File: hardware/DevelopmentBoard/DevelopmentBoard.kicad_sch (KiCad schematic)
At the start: 0 parts

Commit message: Update development board hardware schematic
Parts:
- added A1: ~, symbol ComponentLibrary:ESP32_Devkitc_V4
- added J1: 12V connector, symbol Connector:Barrel_Jack
- added J2: Servo 1, symbol Connector:Conn_01x03_Pin
- added J3: Servo 2, symbol Connector:Conn_01x03_Pin
- added J4: JTAG, symbol Connector_Generic:Conn_02x10_Odd_Even
- added Pot1: 10k, symbol Device:R_Potentiometer
- added R1, R2, R3, R4: 10k, symbol Device:R
- added SW1, SW2, SW3, SW4: SW_Push, symbol Switch:SW_Push
- added TrimPot1, TrimPot2: 10k, symbol Device:R_Potentiometer_Trim
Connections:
- new net: J1.1, J2.2 (Pin_2), J3.2 (Pin_2)
- new net: A1.30 (18), J3.3 (Pin_3)
- new net: A1.10 (26), TrimPot1.2
- new net: A1.11 (27), TrimPot2.2
- new net: A1.12 (14), J4.7 (Pin_7)
- new net: A1.13 (12), J4.5 (Pin_5)
- new net: A1.15 (13), J4.9 (Pin_9)
- new net: A1.2 (EN), J4.3 (Pin_3)
- new net: A1.23 (15), J4.13 (Pin_13)
- new net: A1.3 (VP), R1.2, SW1.2
- new net: A1.31 (19), J2.3 (Pin_3)
- new net: A1.4 (VN), R2.2, SW2.2
- new net: A1.5 (34), R3.2, SW3.2
- new net: A1.6 (35), R4.2, SW4.2
- new net: A1.9 (25), Pot1.2
- new net GND: A1.38 (GND), J1.2, J2.1 (Pin_1), J3.1 (Pin_1), J4.10 (Pin_10), J4.12 (Pin_12), J4.14 (Pin_14), J4.16 (Pin_16), J4.18 (Pin_18), J4.20 (Pin_20), J4.4 (Pin_4), J4.6 (Pin_6), J4.8 (Pin_8), Pot1.3, SW1.1, SW2.1, SW3.1, SW4.1, TrimPot1.3, TrimPot2.3
- new net VCC: A1.1 (3V3), J4.1 (Pin_1), Pot1.1, R1.1, R2.1, R3.1, R4.1, TrimPot1.1, TrimPot2.1
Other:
- company: (none) -> ProstheticHand
- title: (none) -> Mini Test Board

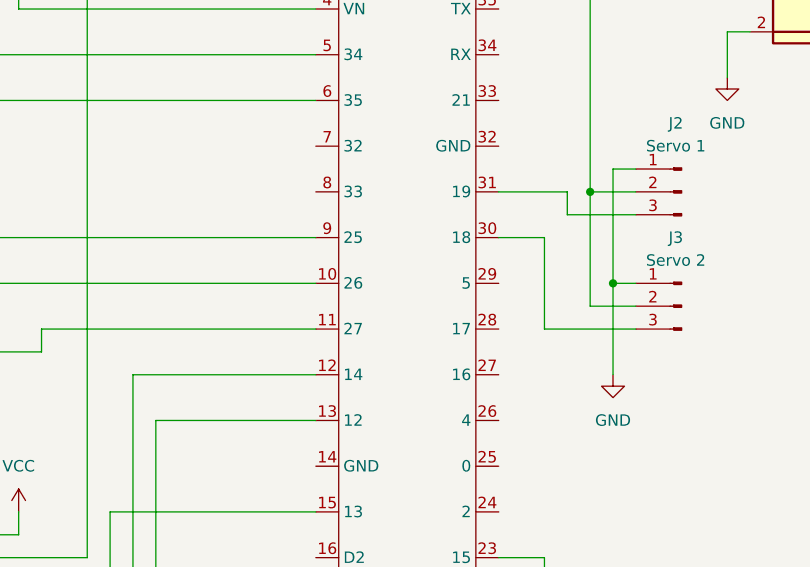
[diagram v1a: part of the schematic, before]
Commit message: Add PCB design for the HW test
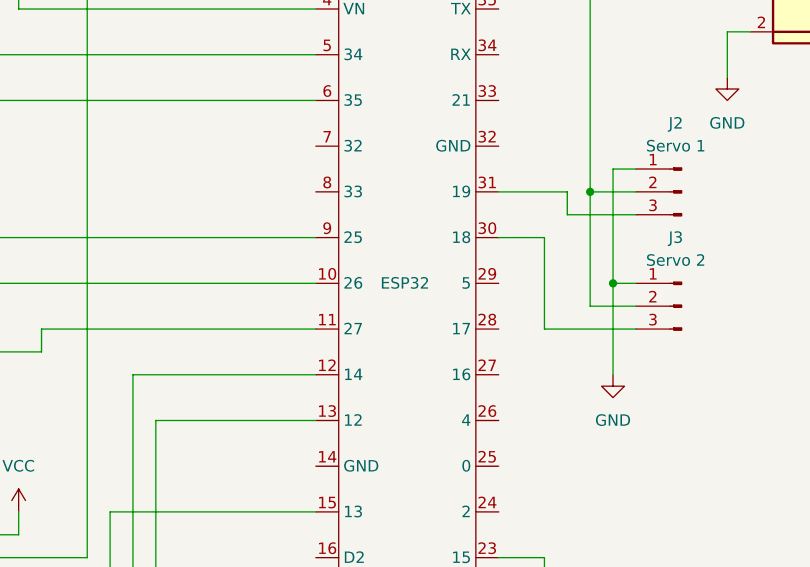
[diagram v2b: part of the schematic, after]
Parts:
- A1: value ~ -> ESP32; footprint (none) -> FootprintLibrary:ICM_ESP32_DevKitC_V4
- J1: footprint (none) -> Connector_BarrelJack:BarrelJack_Horizontal
- J2, J3: footprint (none) -> Connector_PinHeader_2.54mm:PinHeader_1x03_P2.54mm_Vertical
- J4: footprint (none) -> Connector_PinHeader_2.54mm:PinHeader_2x10_P2.54mm_Vertical
- Pot1: footprint (none) -> Potentiometer_THT:Potentiometer_Piher_T-16H_Single_Horizontal
- R1, R2, R3, R4: footprint (none) -> Resistor_THT:R_Axial_DIN0207_L6.3mm_D2.5mm_P7.62mm_Horizontal
- SW1, SW2, SW3, SW4: footprint (none) -> Button_Switch_THT:SW_PUSH_6mm
- TrimPot1, TrimPot2: footprint (none) -> Potentiometer_THT:Potentiometer_Bourns_3386C_Horizontal
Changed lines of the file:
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@@
       (effects (font (size 1.27 1.27)))
     )
-    (property "Footprint" "" (at 233.68 129.54 0)
+    (property "Footprint" "Connector_PinHeader_2.54mm:PinHeader_1x03_P2.54mm_Vertical" (at 233.68 129.54 0)
       (effects (font (size 1.27 1.27)) hide)
     )
@@
       (effects (font (size 1.27 1.27)))
     )
-    (property "Value" "~" (at 202.946 127 0)
-      (effects (font (size 1.27 1.27)))
-    )
-    (property "Footprint" "" (at 202.946 127 0)
+    (property "Value" "ESP32" (at 202.946 127 0)
+      (effects (font (size 1.27 1.27)))
+    )
+    (property "Footprint" "FootprintLibrary:ICM_ESP32_DevKitC_V4" (at 202.946 127 0)
       (effects (font (size 1.27 1.27)) hide)
     )
@@
       (effects (font (size 1.27 1.27)) hide)
     )
-    (property "Footprint" "" (at 91.44 106.68 0)
+    (property "Footprint" "Button_Switch_THT:SW_PUSH_6mm" (at 91.44 106.68 0)
       (effects (font (size 1.27 1.27)) hide)
     )
@@
       (effects (font (size 1.27 1.27)) hide)
     )
-    (property "Footprint" "" (at 91.44 76.2 0)
+    (property "Footprint" "Button_Switch_THT:SW_PUSH_6mm" (at 91.44 76.2 0)
       (effects (font (size 1.27 1.27)) hide)
     )
@@
       (effects (font (size 1.27 1.27)) hide)
     )
-    (property "Footprint" "" (at 91.44 96.52 0)
+    (property "Footprint" "Button_Switch_THT:SW_PUSH_6mm" (at 91.44 96.52 0)
       (effects (font (size 1.27 1.27)) hide)
     )
@@
       (effects (font (size 1.27 1.27)))
     )
-    (property "Footprint" "" (at 233.68 116.84 0)
+    (property "Footprint" "Connector_PinHeader_2.54mm:PinHeader_1x03_P2.54mm_Vertical" (at 233.68 116.84 0)
       (effects (font (size 1.27 1.27)) hide)
     )
@@
       (effects (font (size 1.27 1.27)))
     )
-    (property "Footprint" "" (at 152.4 165.1 0)
+    (property "Footprint" "Connector_PinHeader_2.54mm:PinHeader_2x10_P2.54mm_Vertical" (at 152.4 165.1 0)
       (effects (font (size 1.27 1.27)) hide)
     )
@@
       (effects (font (size 1.27 1.27)) (justify right))
     )
-    (property "Footprint" "" (at 132.08 130.81 0)
+    (property "Footprint" "Potentiometer_THT:Potentiometer_Bourns_3386C_Horizontal" (at 132.08 130.81 0)
       (effects (font (size 1.27 1.27)) hide)
     )
@@
       (effects (font (size 1.27 1.27)) hide)
     )
-    (property "Footprint" "" (at 91.44 86.36 0)
+    (property "Footprint" "Button_Switch_THT:SW_PUSH_6mm" (at 91.44 86.36 0)
       (effects (font (size 1.27 1.27)) hide)
     )
@@
       (effects (font (size 1.27 1.27)) (justify left))
     )
-    (property "Footprint" "" (at 112.522 72.39 90)
+    (property "Footprint" "Resistor_THT:R_Axial_DIN0207_L6.3mm_D2.5mm_P7.62mm_Horizontal" (at 112.522 72.39 90)
       (effects (font (size 1.27 1.27)) hide)
     )
@@
       (effects (font (size 1.27 1.27)) (justify right))
     )
-    (property "Footprint" "" (at 147.32 134.62 0)
+    (property "Footprint" "Potentiometer_THT:Potentiometer_Bourns_3386C_Horizontal" (at 147.32 134.62 0)
       (effects (font (size 1.27 1.27)) hide)
     )
@@
       (effects (font (size 1.27 1.27)) (justify left))
     )
-    (property "Footprint" "" (at 122.682 72.39 90)
+    (property "Footprint" "Resistor_THT:R_Axial_DIN0207_L6.3mm_D2.5mm_P7.62mm_Horizontal" (at 122.682 72.39 90)
       (effects (font (size 1.27 1.27)) hide)
     )
@@
       (effects (font (size 1.27 1.27)) (justify left))
     )
-    (property "Footprint" "" (at 132.842 72.39 90)
+    (property "Footprint" "Resistor_THT:R_Axial_DIN0207_L6.3mm_D2.5mm_P7.62mm_Horizontal" (at 132.842 72.39 90)
       (effects (font (size 1.27 1.27)) hide)
     )
@@
       (effects (font (size 1.27 1.27)))
     )
-    (property "Footprint" "" (at 247.65 97.536 0)
+    (property "Footprint" "Connector_BarrelJack:BarrelJack_Horizontal" (at 247.65 97.536 0)
       (effects (font (size 1.27 1.27)) hide)
     )
@@
       (effects (font (size 1.27 1.27)) (justify left))
     )
-    (property "Footprint" "" (at 102.362 72.39 90)
+    (property "Footprint" "Resistor_THT:R_Axial_DIN0207_L6.3mm_D2.5mm_P7.62mm_Horizontal" (at 102.362 72.39 90)
       (effects (font (size 1.27 1.27)) hide)
     )
@@
       (effects (font (size 1.27 1.27)) (justify right))
     )
-    (property "Footprint" "" (at 116.84 125.73 0)
-      (effects (font (size 1.27 1.27)) hide)
-    )
+    (property "Footprint" "Potentiometer_THT:Potentiometer_Piher_T-16H_Single_Horizontal" (at 116.84 125.73 0)
+      (effects (font (size 1.27 1.27)) hide)
+    )
